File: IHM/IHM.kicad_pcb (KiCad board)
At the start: 2 copper layers, 60 x 60 mm, 21 parts, among them SW1 SW_Push, SW2 SW_Push, SW3 SW_Push, SW4 SW_Push, U1 WeMos_D1_mini

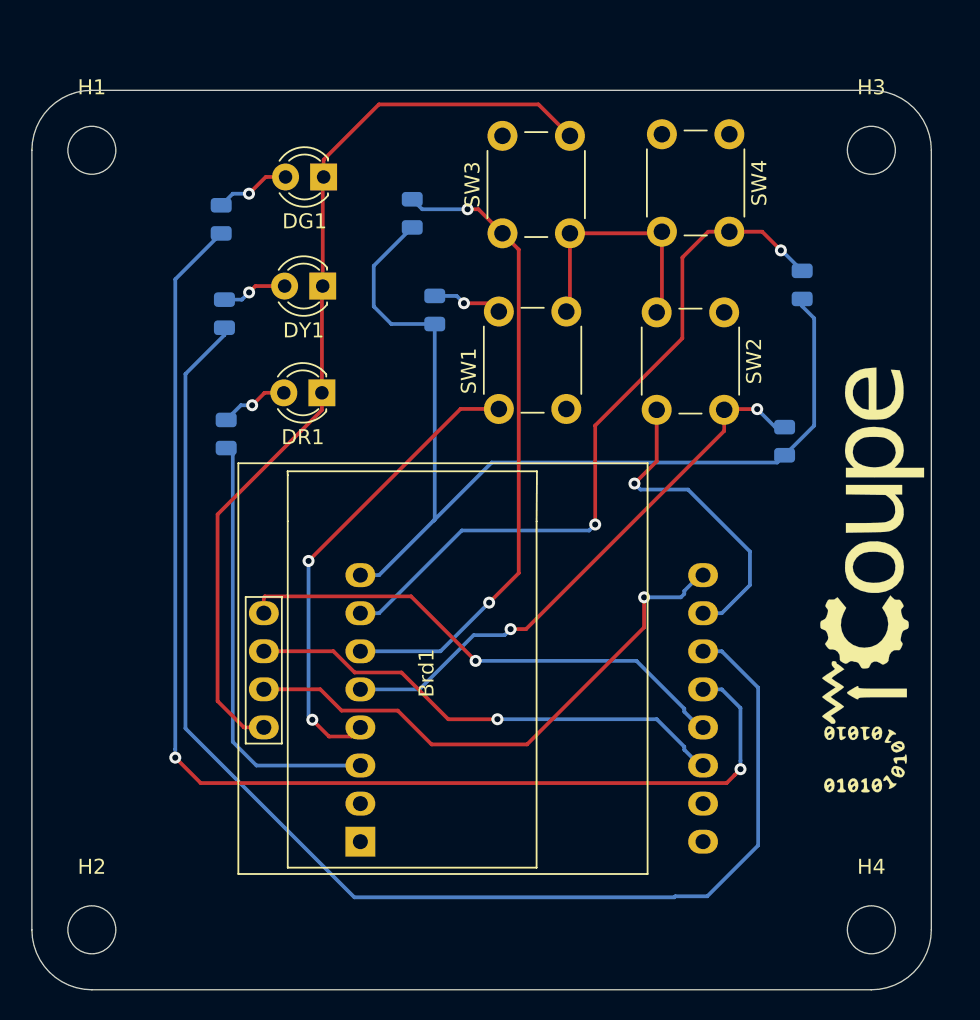
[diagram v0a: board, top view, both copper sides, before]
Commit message: Rotate PCB
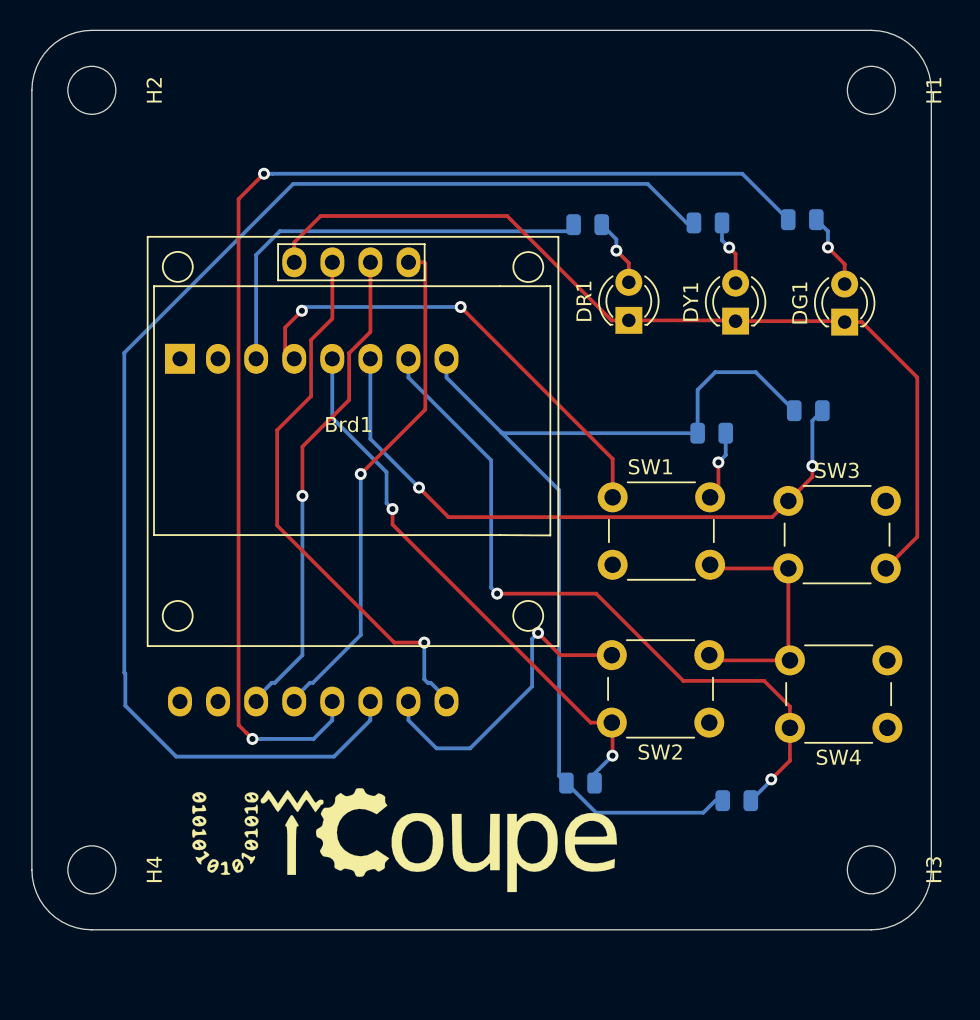
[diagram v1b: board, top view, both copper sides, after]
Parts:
- moved H2 56.0 mm to (104.0, 100.0), turned to 270 degrees
- moved H1 52.2 mm to (156.0, 100.0), turned to 270 degrees
- moved H4 52.2 mm to (104.0, 152.0), turned to 270 degrees
- moved H3 48.0 mm to (156.0, 152.0), turned to 270 degrees
- moved SW4 41.0 mm to (157.1, 142.5), turned to 180 degrees
- moved RG1 38.8 mm to (151.4, 108.6), turned to 180 degrees
- moved DG1 36.1 mm to (154.2, 115.5), turned to 90 degrees
- moved G*** 35.7 mm to (124.8, 150.0), turned to 0 degrees
- moved R4 34.7 mm to (147.0, 147.4), turned to 180 degrees
- moved U1 34.4 mm to (109.9, 117.9), turned to 270 degrees
- moved RY1 32.8 mm to (145.1, 108.8), turned to 180 degrees
- moved R3 29.5 mm to (151.8, 121.4), turned to 180 degrees
- moved RR1 27.9 mm to (137.1, 109.0), turned to 180 degrees
- moved DY1 27.6 mm to (146.9, 115.4), turned to 90 degrees
- moved SW2 27.4 mm to (145.2, 142.2), turned to 180 degrees
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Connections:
- net /Vc renamed +3V3
- DG1 pad 1: /Ground -> GND
- DR1 pad 1: /Ground -> GND
- DY1 pad 1: /Ground -> GND
- SW1 pad 2: /Ground -> GND
- SW2 pad 2: /Ground -> GND
- SW3 pad 2: /Ground -> GND
- SW4 pad 2: /Ground -> GND
- U1 pad 10: /Ground -> GND
- U1 pad 9: /Vcc -> +5V
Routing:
- net /Ground: track 100.0 -> 61.7 mm, vias 1 -> 0
- net GND: track 0.00 -> 38.3 mm, vias 0 -> 1

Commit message: Reroute
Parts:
- removed DY1: LED, LED_THT:LED_D3.0mm
- removed RY1: 330, Resistor_SMD:R_0805_2012Metric
- added C1: 100nF, Capacitor_SMD:C_0603_1608Metric, F.Cu at (130.8, 135.1)
- added C2: 100nF, Capacitor_SMD:C_0603_1608Metric, F.Cu at (130.8, 132.1)
- added C3: 100nF, Capacitor_SMD:C_0603_1608Metric, F.Cu at (148.1, 143.2)
- added C4: 100nF, Capacitor_SMD:C_0603_1608Metric, F.Cu at (130.8, 141.5)
- added C5: 100nF, Capacitor_SMD:C_0603_1608Metric, F.Cu at (130.8, 138.5)
- added J1: JACK, Connector_Phoenix_MC:PhoenixContact_MC_1,5_2-G-3.5_1x02_P3.50mm_Horizontal, B.Cu at (151.6, 141.5)
- added R5: 10k, Resistor_SMD:R_0603_1608Metric, F.Cu at (146.6, 143.2)
- added R6: 4k7, Resistor_SMD:R_0603_1608Metric, F.Cu at (122.0, 116.3)
- added R7: 4k7, Resistor_SMD:R_0603_1608Metric, F.Cu at (117.8, 116.3)
- R1, R2, R3, R4: footprint Resistor_SMD:R_0805_2012Metric -> Resistor_SMD:R_0603_1608Metric; moved to F.Cu
- RG1, RR1: value 330 -> 3k3; footprint Resistor_SMD:R_0805_2012Metric -> Resistor_SMD:R_0603_1608Metric; moved to F.Cu
- SW1: value SW_Push -> BTN_R1
- SW2: value SW_Push -> BTN_L1
- SW3: value SW_Push -> BTN_L2
- SW4: value SW_Push -> BTN_R2
- moved U1 29.2 mm to (126.3, 142.1), turned to 90 degrees
- moved R3 28.0 mm to (132.3, 141.5), turned to 90 degrees
- moved R1 17.9 mm to (132.3, 135.1), turned to 90 degrees
- moved R4 17.2 mm to (132.3, 138.5), turned to 270 degrees
- moved SW4 16.6 mm to (141.3, 137.3), turned to 45 degrees
- moved SW2 15.4 mm to (134.3, 131.3), turned to 45 degrees
- moved R2 14.7 mm to (132.3, 132.1), turned to 270 degrees
- moved RG1 8.72 mm to (148.9, 117.0)
- moved RR1 8.49 mm to (139.9, 117.0)
- moved H1 8.00 mm to (156.0, 108.0)
- moved H2 8.00 mm to (104.0, 108.0)
- moved DG1 5.42 mm to (149.7, 112.5), turned to 270 degrees
- moved Brd1 5.12 mm to (116.5, 124.3)
- moved SW3 4.48 mm to (148.3, 131.3), turned to 45 degrees
- moved SW1 3.15 mm to (141.3, 125.3), turned to 45 degrees
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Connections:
- Brd1 pad 1: /Ground -> GND
- Brd1 pad 2: /Vcc -> +3V3
- R4 pad 1: /D8 -> /D0
- RG1 pad 2: /D3 -> /D8
- RR1 pad 2: /D0 -> /D3
- SW4 pad 1: /D8 -> /D0
- U1 pad 11: Net-(U1-Pad11) -> /D4
- U1 pad 12: Net-(U1-Pad12) -> /D3
- U1 pad 3: Net-(U1-Pad3) -> /D0
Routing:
- net /Ground: track 61.7 -> 0.00 mm
- net /D3: track 82.1 -> 25.8 mm, vias 2 -> 0
- net +3V3: track 67.2 -> 106.7 mm, vias 0 -> 3
- net GND: track 38.3 -> 0.00 mm, vias 1 -> 2
- net /Vcc: track 36.8 -> 0.00 mm, vias 1 -> 0
- net /SDA: track 34.1 -> 6.34 mm, vias 1 -> 0
- net /SCL: track 32.6 -> 10.9 mm, vias 1 -> 0
- net /D4: track 87.3 -> 68.2 mm
- net /D6: track 37.4 -> 29.2 mm, vias 2 -> 0
- net /D7: track 42.8 -> 47.9 mm, vias 2 -> 0
- net Net-(DY1-Pad2): track 4.39 -> 0.00 mm, vias 1 -> 0
- net Net-(DG1-Pad2): track 5.08 -> 1.94 mm, vias 1 -> 0
- net Net-(DR1-Pad2): track 4.59 -> 1.93 mm, vias 1 -> 0
- net /D5: track 36.2 -> 37.1 mm, vias 3 -> 0
- net /D8: track 48.1 -> 47.4 mm, vias 2 -> 0
- added copper zone on B.Cu, net GND
- added copper zone on F.Cu, net GND
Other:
- board size 60 x 60 mm -> 60 x 52 mm

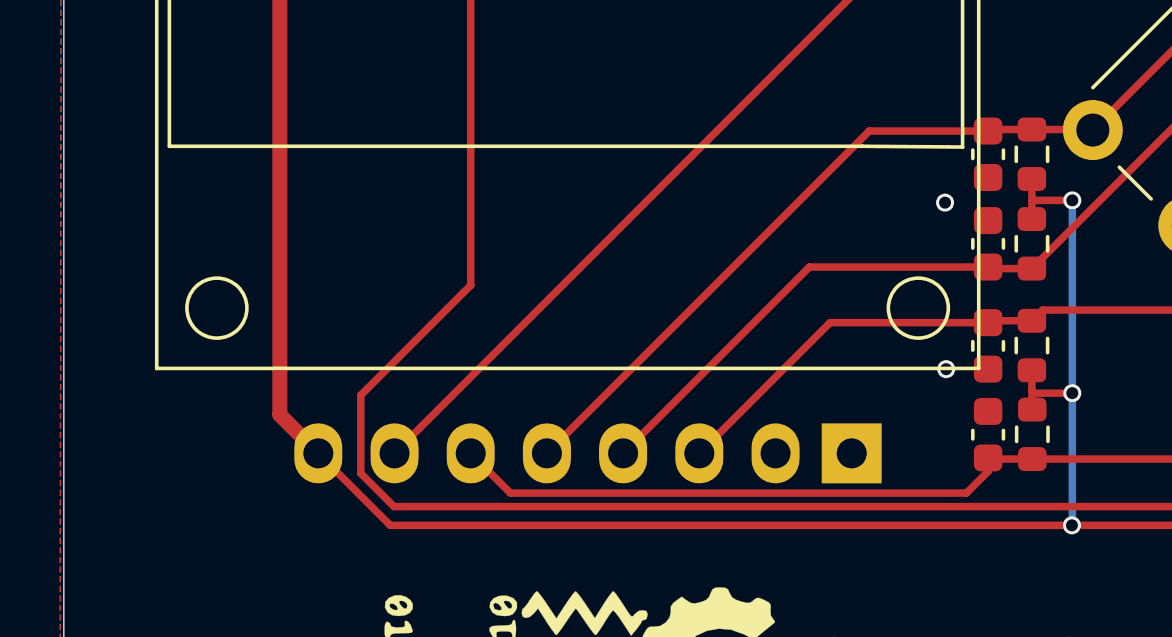
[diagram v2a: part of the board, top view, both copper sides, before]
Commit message: Add mounting holes
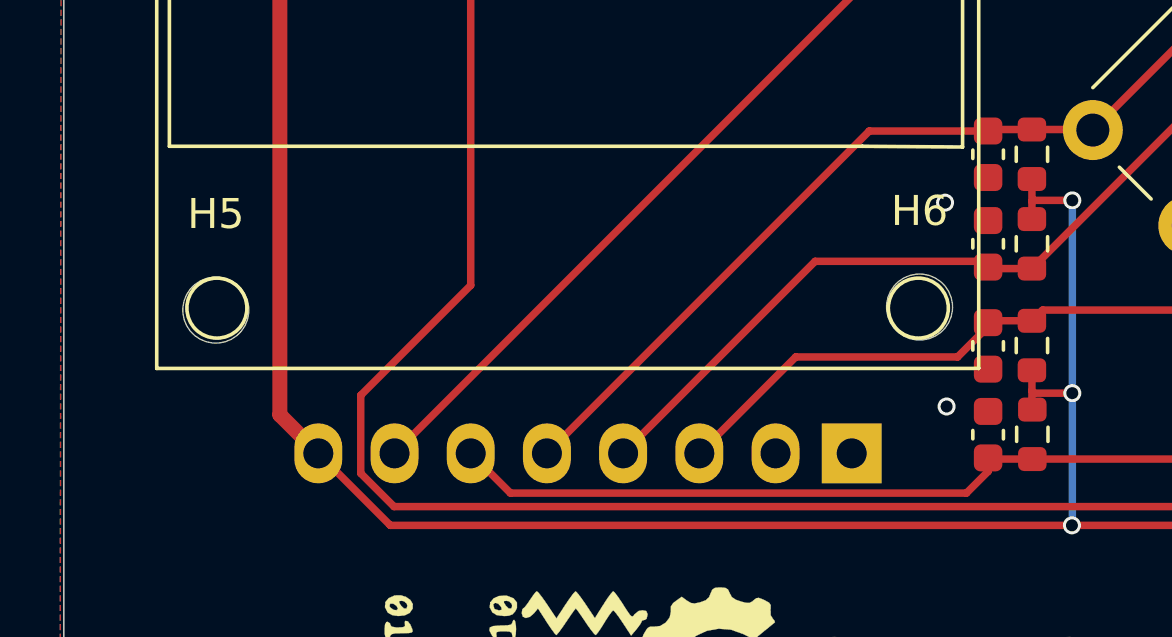
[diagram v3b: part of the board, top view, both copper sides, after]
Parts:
- added H5: MountingHole, MountingHole:MountingHole_2.2mm_M2, F.Cu at (105.1, 137.3)
- added H6: MountingHole, MountingHole:MountingHole_2.2mm_M2, F.Cu at (128.5, 137.2)
- RG1, RR1: value 3k3 -> 1k5
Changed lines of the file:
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@@
     (thickness 1.6)
     (drawings 8)
-    (tracks 98)
+    (tracks 101)
     (zones 0)
-    (modules 28)
+    (modules 30)
     (nets 19)
   )
@@
     (add_net "Net-(U1-Pad2)")
   )
+  (module MountingHole:MountingHole_2.2mm_M2 (layer F.Cu)
+    (at 128.524 137.2108)
+    (descr "Mounting Hole 2.2mm, no annular, M2")
+    (tags "mounting hole 2.2mm no annular m2")
+    (attr virtual)
+    (fp_text reference H6 (at 0 -3.2) (layer F.SilkS)
+      (effects (font (size 1 1) (thickness 0.15)))
+    )
+    (fp_text value MountingHole (at 0 3.2) (layer F.Fab)
+      (effects (font (size 1 1) (thickness 0.15)))
+    )
+    (fp_text user %R (at 0.3 0) (layer F.Fab)
+      (effects (font (size 1 1) (thickness 0.15)))
+    )
+    (fp_circle (center 0 0) (end 2.2 0) (layer Cmts.User) (width 0.15))
+    (fp_circle (center 0 0) (end 2.45 0) (layer F.CrtYd) (width 0.05))
+    (pad 1 np_thru_hole circle (at 0 0) (size 2.2 2.2) (drill 2.2) (layers *.Cu *.Mask))
+  )
+  (module MountingHole:MountingHole_2.2mm_M2 (layer F.Cu)
+    (at 105.0671 137.3124)
+    (descr "Mounting Hole 2.2mm, no annular, M2")
+    (tags "mounting hole 2.2mm no annular m2")
+    (attr virtual)
+    (fp_text reference H5 (at 0 -3.2) (layer F.SilkS)
+      (effects (font (size 1 1) (thickness 0.15)))
+    )
+    (fp_text value MountingHole (at 0 3.2) (layer F.Fab)
+      (effects (font (size 1 1) (thickness 0.15)))
+    )
+    (fp_text user %R (at 0.3 0) (layer F.Fab)
+      (effects (font (size 1 1) (thickness 0.15)))
+    )
+    (fp_circle (center 0 0) (end 2.2 0) (layer Cmts.User) (width 0.15))
+    (fp_circle (center 0 0) (end 2.45 0) (layer F.CrtYd) (width 0.05))
+    (pad 1 np_thru_hole circle (at 0 0) (size 2.2 2.2) (drill 2.2) (layers *.Cu *.Mask))
+  )
+  (module UTCoupe:128x64OLED (layer F.Cu)
+    (at 116.4971 124.2568)
+    (fp_text reference Brd1 (at 0 0.254) (layer F.SilkS) hide
+      (effects (font (size 1 1) (thickness 0.15)))
+    )
+    (fp_text value SSD1306 (at -7.747 -7.62) (layer F.Fab)
+      (effects (font (size 1 1) (thickness 0.15)))
+    )
+    (fp_circle (center 11.98676 12.98956) (end 12.98676 12.98956) (layer F.SilkS) (width 0.12))
+    (fp_circle (center -11.39444 12.98956) (end -10.39444 12.98956) (layer F.SilkS) (width 0.12))
+    (fp_circle (center -11.38936 -10.29512) (end -10.38936 -10.29512) (layer F.SilkS) (width 0.12))
+    (fp_circle (center 11.99032 -10.28344) (end 12.99032 -10.28344) (layer F.SilkS) (width 0.12))
+    (fp_line (start 13.462 -9.017) (end 13.208 -9.005) (layer F.SilkS) (width 0.12))
+    (fp_line (start 13.462 7.62) (end 13.462 -9.017) (layer F.SilkS) (width 0.12))
+    (fp_line (start 10.122 7.595) (end 13.462 7.62) (layer F.SilkS) (width 0.12))
+    (fp_line (start 10.122 -9.005) (end 13.208 -9.005) (layer F.SilkS) (width 0.12))
+    (fp_line (start -4.699 -11.811) (end -4.699 -9.398) (layer F.SilkS) (width 0.12))
+    (fp_line (start 5.08 -9.398) (end -4.699 -9.398) (layer F.SilkS) (width 0.12))
+    (fp_line (start 5.08 -11.811) (end 5.08 -9.398) (layer F.SilkS) (width 0.12))
+    (fp_line (start -4.699 -11.811) (end 5.08 -11.811) (layer F.SilkS) (width 0.12))
+    (fp_line (start -12.978 -9.005) (end 10.122 -9.005) (layer F.SilkS) (width 0.12))
+    (fp_line (start -12.978 7.595) (end -12.978 -9.005) (layer F.SilkS) (width 0.12))
+    (fp_line (start 10.122 7.595) (end -12.978 7.595) (layer F.SilkS) (width 0.12))
+    (fp_line (start -13.4 15) (end -13.4 -12.3) (layer F.SilkS) (width 0.12))
+    (fp_line (start 14 15) (end -13.4 15) (layer F.SilkS) (width 0.12))
+    (fp_line (start 14 -12.3) (end 14 15) (layer F.SilkS) (width 0.12))
+    (fp_line (start -13.4 -12.3) (end 14 -12.3) (layer F.SilkS) (width 0.12))
+    (pad 2 thru_hole oval (at -1.08 -10.6 90) (size 2 1.6) (drill 1) (layers *.Cu *.Mask)
+      (net 17 +3V3))
+    (pad 1 thru_hole oval (at -3.62 -10.6 90) (size 2 1.6) (drill 1) (layers *.Cu *.Mask)
+      (net 16 GND))
+    (pad 3 thru_hole oval (at 1.46 -10.6 90) (size 2 1.6) (drill 1) (layers *.Cu *.Mask)
+      (net 1 /SCL))
+    (pad 4 thru_hole oval (at 4 -10.6 90) (size 2 1.6) (drill 1) (layers *.Cu *.Mask)
+      (net 2 /SDA))
+    (model ${UTCOUPE3D}/OLED-128x64-0.96.step
+      (offset (xyz 34.5 3.5 10.5))
+      (scale (xyz 1 1 1))
+      (rotate (xyz 0 0 0))
+    )
+  )
   (module Capacitor_SMD:C_0603_1608Metric (layer F.Cu)
     (at 130.81 141.4653 90)
@@
       (effects (font (size 1 1) (thickness 0.15)))
     )
-    (fp_text value 3k3 (at 0 1.43) (layer F.Fab)
+    (fp_text value 1k5 (at 0 1.43) (layer F.Fab)
       (effects (font (size 1 1) (thickness 0.15)))
     )
@@
       (effects (font (size 1 1) (thickness 0.15)))
     )
-    (fp_text value 3k3 (at 0 1.43) (layer F.Fab)
+    (fp_text value 1k5 (at 0 1.43) (layer F.Fab)
       (effects (font (size 1 1) (thickness 0.15)))
     )
@@
       (rotate (xyz 0 0 0))
     )
-  )
-  (module UTCoupe:128x64OLED (layer F.Cu)
-    (at 116.4971 124.2568)
-    (fp_text reference Brd1 (at 0 0.254) (layer F.SilkS) hide
-      (effects (font (size 1 1) (thickness 0.15)))
-    )
-    (fp_text value SSD1306 (at -7.747 -7.62) (layer F.Fab)
-      (effects (font (size 1 1) (thickness 0.15)))
-    )
-    (fp_line (start -13.4 -12.3) (end 14 -12.3) (layer F.SilkS) (width 0.12))
-    (fp_line (start 14 -12.3) (end 14 15) (layer F.SilkS) (width 0.12))
-    (fp_line (start 14 15) (end -13.4 15) (layer F.SilkS) (width 0.12))
-    (fp_line (start -13.4 15) (end -13.4 -12.3) (layer F.SilkS) (width 0.12))
-    (fp_line (start 10.122 7.595) (end -12.978 7.595) (layer F.SilkS) (width 0.12))
-    (fp_line (start -12.978 7.595) (end -12.978 -9.005) (layer F.SilkS) (width 0.12))
-    (fp_line (start -12.978 -9.005) (end 10.122 -9.005) (layer F.SilkS) (width 0.12))
-    (fp_line (start -4.699 -11.811) (end 5.08 -11.811) (layer F.SilkS) (width 0.12))
-    (fp_line (start 5.08 -11.811) (end 5.08 -9.398) (layer F.SilkS) (width 0.12))
-    (fp_line (start 5.08 -9.398) (end -4.699 -9.398) (layer F.SilkS) (width 0.12))
-    (fp_line (start -4.699 -11.811) (end -4.699 -9.398) (layer F.SilkS) (width 0.12))
-    (fp_line (start 10.122 -9.005) (end 13.208 -9.005) (layer F.SilkS) (width 0.12))
-    (fp_line (start 10.122 7.595) (end 13.462 7.62) (layer F.SilkS) (width 0.12))
-    (fp_line (start 13.462 7.62) (end 13.462 -9.017) (layer F.SilkS) (width 0.12))
-    (fp_line (start 13.462 -9.017) (end 13.208 -9.005) (layer F.SilkS) (width 0.12))
-    (fp_circle (center 11.99032 -10.28344) (end 12.99032 -10.28344) (layer F.SilkS) (width 0.12))
-    (fp_circle (center -11.38936 -10.29512) (end -10.38936 -10.29512) (layer F.SilkS) (width 0.12))
-    (fp_circle (center -11.39444 12.98956) (end -10.39444 12.98956) (layer F.SilkS) (width 0.12))
-    (fp_circle (center 11.98676 12.98956) (end 12.98676 12.98956) (layer F.SilkS) (width 0.12))
-    (pad 2 thru_hole oval (at -1.08 -10.6 90) (size 2 1.6) (drill 1) (layers *.Cu *.Mask)
-      (net 17 +3V3))
-    (pad 1 thru_hole oval (at -3.62 -10.6 90) (size 2 1.6) (drill 1) (layers *.Cu *.Mask)
-      (net 16 GND))
-    (pad 3 thru_hole oval (at 1.46 -10.6 90) (size 2 1.6) (drill 1) (layers *.Cu *.Mask)
-      (net 1 /SCL))
-    (pad 4 thru_hole oval (at 4 -10.6 90) (size 2 1.6) (drill 1) (layers *.Cu *.Mask)
-      (net 2 /SDA))
   )
   (module UTCoupe:logo_UTCoupe_Medium locked (layer F.Cu)
@@
   (segment (start 132.6277 137.3113) (end 132.2705 137.6685) (width 0.25) (layer F.Cu) (net 6))
   (segment (start 141.3006 137.3113) (end 132.6277 137.3113) (width 0.25) (layer F.Cu) (net 6))
-  (segment (start 125.5398 137.7312) (end 121.1834 142.0876) (width 0.25) (layer F.Cu) (net 6))
-  (segment (start 130.81 137.7312) (end 125.5398 137.7312) (width 0.25) (layer F.Cu) (net 6))
+  (segment (start 129.794 138.8745) (end 124.3965 138.8745) (width 0.25) (layer F.Cu) (net 6))
+  (segment (start 130.81 137.7312) (end 130.81 137.8585) (width 0.25) (layer F.Cu) (net 6))
+  (segment (start 124.3965 138.8745) (end 121.1834 142.0876) (width 0.25) (layer F.Cu) (net 6))
+  (segment (start 130.81 137.8585) (end 129.794 138.8745) (width 0.25) (layer F.Cu) (net 6))
   (segment (start 149.0925 141.4578) (end 148.0947 142.4556) (width 0.25) (layer F.Cu) (net 7))
   (segment (start 151.5618 141.4578) (end 149.0925 141.4578) (width 0.25) (layer F.Cu) (net 7))
@@
   (segment (start 132.2705 135.9276) (end 130.86 135.9276) (width 0.25) (layer F.Cu) (net 8))
   (segment (start 145.896794 120.715106) (end 141.3006 125.3113) (width 0.25) (layer F.Cu) (net 8))
-  (segment (start 124.8534 135.8776) (end 118.6434 142.0876) (width 0.25) (layer F.Cu) (net 8))
-  (segment (start 130.81 135.8776) (end 124.8534 135.8776) (width 0.25) (layer F.Cu) (net 8))
   (segment (start 141.3006 126.8975) (end 141.3006 125.3113) (width 0.25) (layer F.Cu) (net 8))
   (segment (start 132.2705 135.9276) (end 141.3006 126.8975) (width 0.25) (layer F.Cu) (net 8))
+  (segment (start 125.0442 135.6868) (end 118.6434 142.0876) (width 0.25) (layer F.Cu) (net 8))
+  (segment (start 130.81 135.8776) (end 130.6192 135.6868) (width 0.25) (layer F.Cu) (net 8))
+  (segment (start 130.6192 135.6868) (end 125.0442 135.6868) (width 0.25) (layer F.Cu) (net 8))
   (segment (start 134.3006 131.3113) (end 138.896794 126.715106) (width 0.25) (layer F.Cu) (net 9))
   (segment (start 130.86 131.2931) (end 130.81 131.3431) (width 0.25) (layer F.Cu) (net 9))
@@
   (segment (start 147.27169 117.77971) (end 135.33129 117.77971) (width 0.25) (layer F.Cu) (net 11))
   (segment (start 148.0717 116.9797) (end 147.27169 117.77971) (width 0.25) (layer F.Cu) (net 11))
-  (via (at 129.413 139.2809) (size 0.6) (drill 0.4) (layers F.Cu B.Cu) (net 16))
+  (via (at 129.4257 140.5255) (size 0.6) (drill 0.4) (layers F.Cu B.Cu) (net 16))
   (via (at 129.3749 133.731) (size 0.6) (drill 0.4) (layers F.Cu B.Cu) (net 16))
   (segment (start 115.4171 114.7435) (end 116.9929 116.3193) (width 0.25) (layer F.Cu) (net 17))
